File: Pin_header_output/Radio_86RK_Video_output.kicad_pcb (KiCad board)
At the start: 2 copper layers, 34.3 x 20.8 mm, 9 parts, among them J1 Conn_01x05, Q1 2N3904

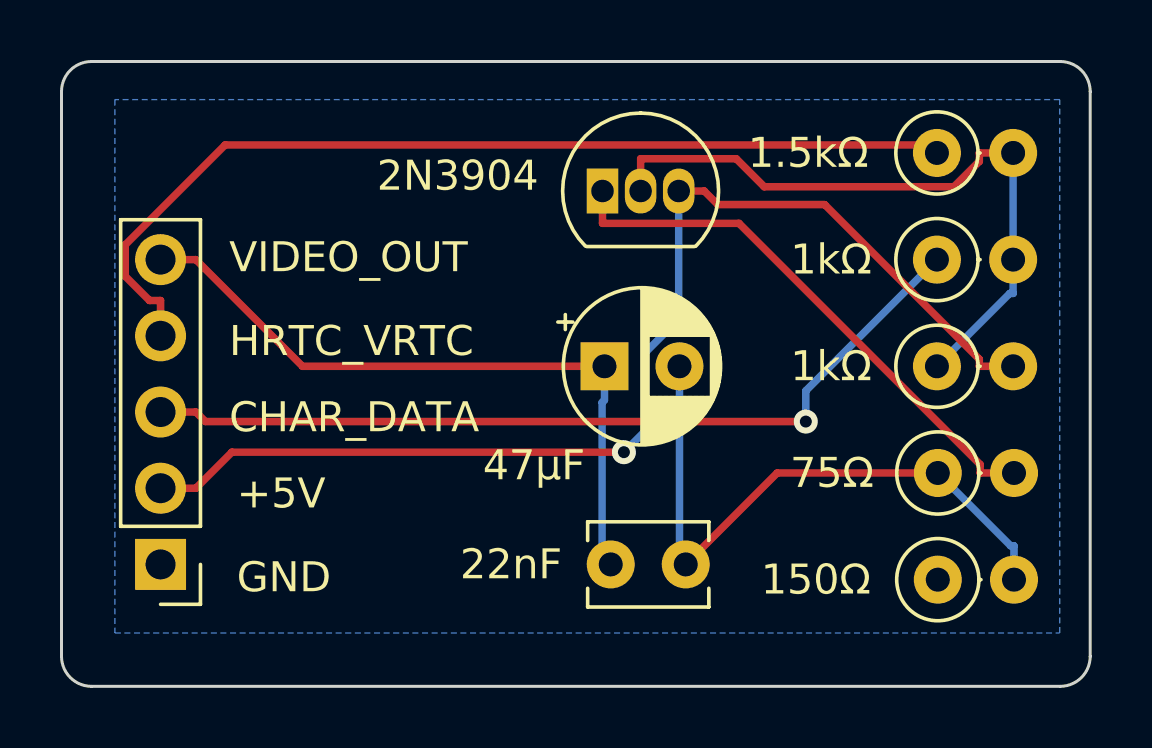
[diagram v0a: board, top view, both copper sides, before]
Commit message: Added mounting hole
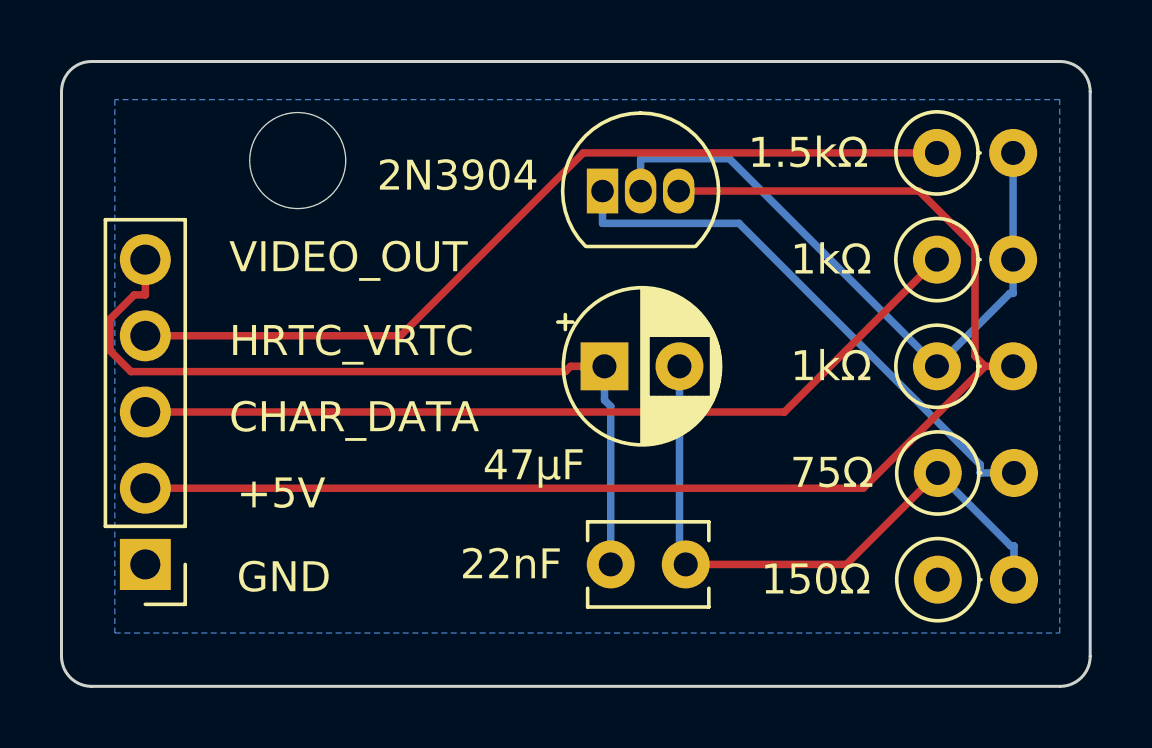
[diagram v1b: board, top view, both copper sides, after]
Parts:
- added H1: MountingHole, MountingHole:MountingHole_3.2mm_M3, F.Cu at (111.3, 70.1)
- moved J1 0.51 mm to (106.2, 83.6)
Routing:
- net 5V: track 39.1 -> 45.4 mm, vias 1 -> 0
- net VIDEO_OUT: track 23.0 -> 27.3 mm
- net HRTC_VRTC: track 32.3 -> 28.9 mm
- net Net-(Q1-B): track 22.7 -> 22.0 mm
- net CHAR_DATA: track 28.8 -> 28.5 mm, vias 1 -> 0

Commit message: Changed HRTC_VRTC to CRTC
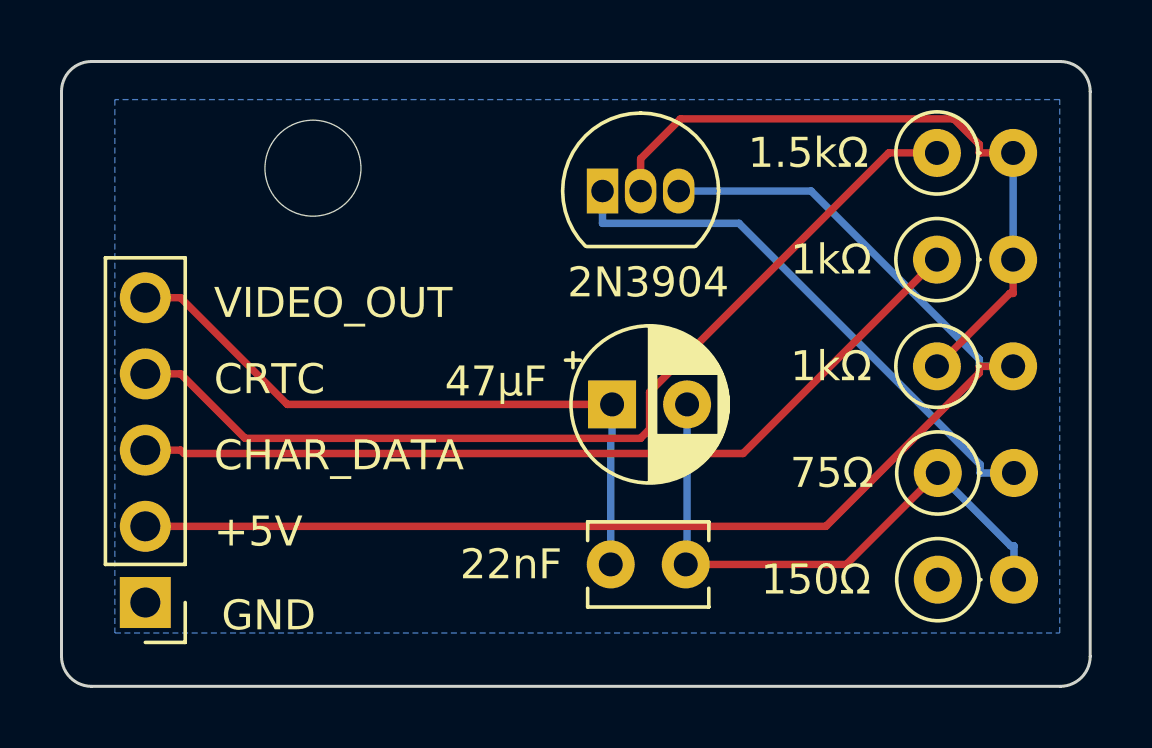
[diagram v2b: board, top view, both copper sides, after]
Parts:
- moved C2 1.30 mm to (121.7, 78.2)
- moved J1 1.27 mm to (106.2, 84.8)
- moved H1 0.57 mm to (111.8, 70.4)
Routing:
- net VIDEO_OUT: track 27.3 -> 22.4 mm
- net HRTC_VRTC: track 28.9 -> 31.9 mm
- net Net-(C1-Pad1): track 21.0 -> 19.7 mm
- net Net-(Q1-B): track 22.0 -> 22.9 mm
- net CHAR_DATA: track 28.5 -> 29.1 mm
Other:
- board text added: "CRTC"
- board text removed: "HRTC_VRTC"
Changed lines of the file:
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@@
 		)
 		(property "Value" "2N3904"
-			(at -4.826 -0.508 0)
+			(at 1.524 3.048 0)
 			(layer "F.SilkS")
 			(effects
@@
 	(footprint "MountingHole:MountingHole_3.2mm_M3"
 		(layer "F.Cu")
-		(at 111.252 70.104)
+		(at 111.76 70.358)
 		(descr "Mounting Hole 3.2mm, no annular, M3")
 		(tags "mounting hole 3.2mm no annular m3")
@@
 	(footprint "Capacitor_THT:CP_Radial_D5.0mm_P2.50mm"
 		(layer "F.Cu")
-		(at 121.4769 76.962)
+		(at 121.7309 78.232)
 		(descr "CP, Radial series, Radial, pin pitch=2.50mm, , diameter=5mm, Electrolytic Capacitor")
 		(tags "CP Radial series Radial pin pitch 2.50mm  diameter 5mm Electrolytic Capacitor")
@@
 		)
 		(property "Value" "47µF"
-			(at -2.3509 3.302 0)
+			(at -3.8749 -0.762 0)
 			(layer "F.SilkS")
 			(effects
@@
 	(footprint "Connector_PinHeader_2.54mm:PinHeader_1x05_P2.54mm_Vertical"
 		(layer "F.Cu")
-		(at 106.172 83.566 180)
+		(at 106.172 84.836 180)
 		(descr "Through hole straight pin header, 1x05, 2.54mm pitch, single row")
 		(tags "Through hole pin header THT 1x05 2.54mm single row")
@@
 	)
 	(gr_text "+5V"
-		(at 109.22 81.788 0)
+		(at 108.458 83.058 0)
 		(layer "F.SilkS")
 		(effects
@@
 	)
 	(gr_text "GND"
-		(at 109.22 84.582 0)
+		(at 108.712 85.852 0)
 		(layer "F.SilkS")
 		(effects
@@
 	)
 	(gr_text "CHAR_DATA"
-		(at 108.966 79.248 0)
+		(at 108.458 80.518 0)
 		(layer "F.SilkS")
 		(effects
@@
 		)
 	)
-	(gr_text "HRTC_VRTC"
-		(at 108.966 76.708 0)
+	(gr_text "CRTC"
+		(at 108.458 77.978 0)
 		(layer "F.SilkS")
 		(effects
@@
 	)
 	(gr_text "VIDEO_OUT"
-		(at 108.966 73.914 0)
+		(at 108.458 75.438 0)
 		(layer "F.SilkS")
 		(effects
@@
 	)
 	(segment
-		(start 132.588 80.518)
-		(end 129.54 83.566)
+		(start 129.54 83.566)
+		(end 124.186 83.566)
 		(width 0.25)
 		(layer "F.Cu")
@@
 	)
 	(segment
-		(start 129.54 83.566)
-		(end 124.186 83.566)
+		(start 132.588 80.518)
+		(end 129.54 83.566)
 		(width 0.25)
 		(layer "F.Cu")
@@
 	)
 	(segment
-		(start 123.9769 76.962)
-		(end 123.9769 83.3569)
+		(start 132.588 80.518)
+		(end 135.0173 82.9473)
 		(width 0.25)
 		(layer "B.Cu")
@@
 	)
 	(segment
-		(start 123.9769 83.3569)
-		(end 124.186 83.566)
+		(start 124.2309 78.232)
+		(end 124.2309 83.5211)
 		(width 0.25)
 		(layer "B.Cu")
@@
 	)
 	(segment
-		(start 132.588 80.518)
-		(end 135.0173 82.9473)
+		(start 135.128 84.074)
+		(end 135.128 82.9473)
 		(width 0.25)
 		(layer "B.Cu")
@@
 	)
 	(segment
-		(start 135.128 84.074)
-		(end 135.128 82.9473)
+		(start 124.2309 83.5211)
+		(end 124.186 83.566)
 		(width 0.25)
 		(layer "B.Cu")
@@
 	)
 	(segment
-		(start 133.829 76.6235)
-		(end 133.829 72.9829)
+		(start 133.9723 76.962)
+		(end 133.9723 77.1845)
 		(width 0.25)
 		(layer "F.Cu")
@@
 	)
 	(segment
-		(start 130.1035 81.026)
-		(end 134.1675 76.962)
+		(start 135.099 76.962)
+		(end 133.9723 76.962)
 		(width 0.25)
 		(layer "F.Cu")
@@
 	)
 	(segment
-		(start 106.172 81.026)
-		(end 130.1035 81.026)
+		(start 128.8608 82.296)
+		(end 106.172 82.296)
 		(width 0.25)
 		(layer "F.Cu")
@@
 	)
 	(segment
-		(start 133.829 72.9829)
-		(end 131.9661 71.12)
+		(start 133.9723 77.1845)
+		(end 128.8608 82.296)
 		(width 0.25)
 		(layer "F.Cu")
@@
 	(segment
 		(start 135.099 76.962)
-		(end 134.1675 76.962)
+		(end 133.9723 76.962)
 		(width 0.25)
-		(layer "F.Cu")
+		(layer "B.Cu")
 		(net 3)
 	)
 	(segment
-		(start 134.1675 76.962)
-		(end 133.829 76.6235)
+		(start 133.9723 76.7253)
+		(end 128.367 71.12)
 		(width 0.25)
-		(layer "F.Cu")
+		(layer "B.Cu")
 		(net 3)
 	)
 	(segment
-		(start 131.9661 71.12)
+		(start 133.9723 76.962)
+		(end 133.9723 76.7253)
+		(width 0.25)
+		(layer "B.Cu")
+		(net 3)
+	)
+	(segment
+		(start 128.367 71.12)
 		(end 123.952 71.12)
 		(width 0.25)
-		(layer "F.Cu")
+		(layer "B.Cu")
 		(net 3)
 	)
 	(segment
-		(start 127.479 78.486)
-		(end 106.172 78.486)
+		(start 106.172 79.756)
+		(end 107.3487 79.756)
+		(width 0.25)
+		(layer "F.Cu")
+		(net 4)
+	)
+	(segment
+		(start 126.0961 79.8689)
+		(end 132.559 73.406)
+		(width 0.25)
+		(layer "F.Cu")
+		(net 4)
+	)
+	(segment
+		(start 107.4616 79.8689)
+		(end 126.0961 79.8689)
 		(width 0.25)
 		(layer "F.Cu")
@@
 	)
 	(segment
-		(start 132.559 73.406)
-		(end 127.479 78.486)
+		(start 107.3487 79.756)
+		(end 107.4616 79.8689)
 		(width 0.25)
 		(layer "F.Cu")
@@
 	)
 	(segment
-		(start 114.6757 75.946)
-		(end 120.7717 69.85)
+		(start 122.9809 79.0595)
+		(end 122.9809 77.8201)
+		(width 0.25)
+		(layer "F.Cu")
+		(net 5)
+	)
+	(segment
+		(start 107.3487 77.216)
+		(end 109.4948 79.3621)
 		(width 0.25)
 		(layer "F.Cu")
@@
 	)
 	(segment
-		(start 120.7717 69.85)
+		(start 106.172 77.216)
+		(end 107.3487 77.216)
+		(width 0.25)
+		(layer "F.Cu")
+		(net 5)
+	)
+	(segment
+		(start 130.951 69.85)
 		(end 132.559 69.85)
 		(width 0.25)
@@
 	)
 	(segment
-		(start 106.172 75.946)
-		(end 114.6757 75.946)
+		(start 122.9809 77.8201)
+		(end 130.951 69.85)
+		(width 0.25)
+		(layer "F.Cu")
+		(net 5)
+	)
+	(segment
+		(start 109.4948 79.3621)
+		(end 122.6783 79.3621)
+		(width 0.25)
+		(layer "F.Cu")
+		(net 5)
+	)
+	(segment
+		(start 122.6783 79.3621)
+		(end 122.9809 79.0595)
 		(width 0.25)
 		(layer "F.Cu")
@@
 	)
 	(segment
-		(start 134.0013 80.2362)
+		(start 121.412 72.1967)
 		(end 125.9618 72.1967)
 		(width 0.25)
@@
 	)
 	(segment
-		(start 134.0013 80.518)
+		(start 125.9618 72.1967)
 		(end 134.0013 80.2362)
 		(width 0.25)
@@
 	)
 	(segment
-		(start 125.9618 72.1967)
-		(end 121.412 72.1967)
+		(start 134.0013 80.2362)
+		(end 134.0013 80.518)
 		(width 0.25)
 		(layer "B.Cu")
@@
 	)
 	(segment
-		(start 125.6403 70.0433)
+		(start 122.682 71.12)
 		(end 122.682 70.0433)
 		(width 0.25)
-		(layer "B.Cu")
-		(net 7)
-	)
-	(segment
-		(start 135.099 73.406)
-		(end 135.099 69.85)
-		(width 0.25)
-		(layer "B.Cu")
+		(layer "F.Cu")
 		(net 7)
 	)
 	(segment
-		(start 132.559 76.962)
-		(end 125.6403 70.0433)
+		(start 135.099 69.85)
+		(end 133.9723 69.85)
 		(width 0.25)
-		(layer "B.Cu")
+		(layer "F.Cu")
 		(net 7)
 	)
 	(segment
-		(start 132.559 76.962)
-		(end 134.9883 74.5327)
+		(start 133.1203 68.7163)
+		(end 124.009 68.7163)
 		(width 0.25)
-		(layer "B.Cu")
+		(layer "F.Cu")
 		(net 7)
 	)
 	(segment
-		(start 122.682 71.12)
-		(end 122.682 70.0433)
+		(start 133.9723 69.85)
+		(end 133.9723 69.5683)
 		(width 0.25)
-		(layer "B.Cu")
+		(layer "F.Cu")
 		(net 7)
 	)
 	(segment
-		(start 134.9883 74.5327)
-		(end 135.099 74.5327)
+		(start 133.9723 69.5683)
+		(end 133.1203 68.7163)
 		(width 0.25)
-		(layer "B.Cu")
+		(layer "F.Cu")
 		(net 7)
 	)
 	(segment
-		(start 135.099 73.9693)
+		(start 135.099 73.406)
 		(end 135.099 74.5327)
 		(width 0.25)
-		(layer "B.Cu")
-		(net 7)
-	)
-	(segment
-		(start 135.099 73.9693)
-		(end 135.099 73.406)
-		(width 0.25)
-		(layer "B.Cu")
-		(net 7)
-	)
-	(segment
-		(start 106.172 73.406)
-		(end 106.172 74.5827)
-		(width 0.25)
 		(layer "F.Cu")
-		(net 8)
+		(net 7)
 	)
 	(segment
-		(start 105.8042 74.5827)
-		(end 106.172 74.5827)
+		(start 132.559 76.962)
+		(end 134.9883 74.5327)
 		(width 0.25)
 		(layer "F.Cu")
-		(net 8)
+		(net 7)
 	)
 	(segment
-		(start 120.1735 77.1387)
-		(end 105.6933 77.1387)
+		(start 124.009 68.7163)
+		(end 122.682 70.0433)
 		(width 0.25)
 		(layer "F.Cu")
-		(net 8)
+		(net 7)
 	)
 	(segment
-		(start 105.6933 77.1387)
-		(end 104.9953 76.4407)
+		(start 134.9883 74.5327)
+		(end 135.099 74.5327)
 		(width 0.25)
 		(layer "F.Cu")
-		(net 8)
+		(net 7)
 	)
 	(segment
-		(start 120.3502 76.962)
-		(end 120.1735 77.1387)
+		(start 135.099 73.406)
+		(end 135.099 69.85)
 		(width 0.25)
-		(layer "F.Cu")
-		(net 8)
+		(layer "B.Cu")
+		(net 7)
 	)
 	(segment
-		(start 104.9953 76.4407)
-		(end 104.9953 75.3916)
+		(start 110.9047 78.232)
+		(end 107.3487 74.676)
 		(width 0.25)
 		(layer "F.Cu")
@@
 	)
 	(segment
-		(start 121.4769 76.962)
-		(end 120.3502 76.962)
+		(start 106.172 74.676)
+		(end 107.3487 74.676)
 		(width 0.25)
 		(layer "F.Cu")
@@
 	)
 	(segment
-		(start 104.9953 75.3916)
-		(end 105.8042 74.5827)
+		(start 121.7309 78.232)
+		(end 110.9047 78.232)
 		(width 0.25)
 		(layer "F.Cu")
@@
 	)
 	(segment
-		(start 121.4769 76.962)
-		(end 121.4769 78.0887)
+		(start 121.686 79.4036)
+		(end 121.686 83.566)
 		(width 0.25)
 		(layer "B.Cu")
@@
 	)
 	(segment
-		(start 121.4769 78.0887)
-		(end 121.686 78.2978)
+		(start 121.7309 79.3587)
+		(end 121.686 79.4036)
 		(width 0.25)
 		(layer "B.Cu")
@@
 	)
 	(segment
-		(start 121.686 78.2978)
-		(end 121.686 83.566)
+		(start 121.7309 78.232)
+		(end 121.7309 79.3587)
 		(width 0.25)
 		(layer "B.Cu")
